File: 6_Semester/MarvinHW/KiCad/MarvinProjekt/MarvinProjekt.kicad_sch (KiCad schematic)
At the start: 27 parts, among them J1 Conn_02x03_Odd_Even, J2 Conn_01x04_Pin, SW1 SW_DPST_x2, SW2 SW_DPST_x2, SW3 SW_DPST_x2, SW4 SW_DPST_x2, SW5 SW_DPST_x2, SW6 SW_DPST_x2, U1 ESP32-S3-WROOM-1, U9 WS2812, X1 USB3.1C16PFSMT

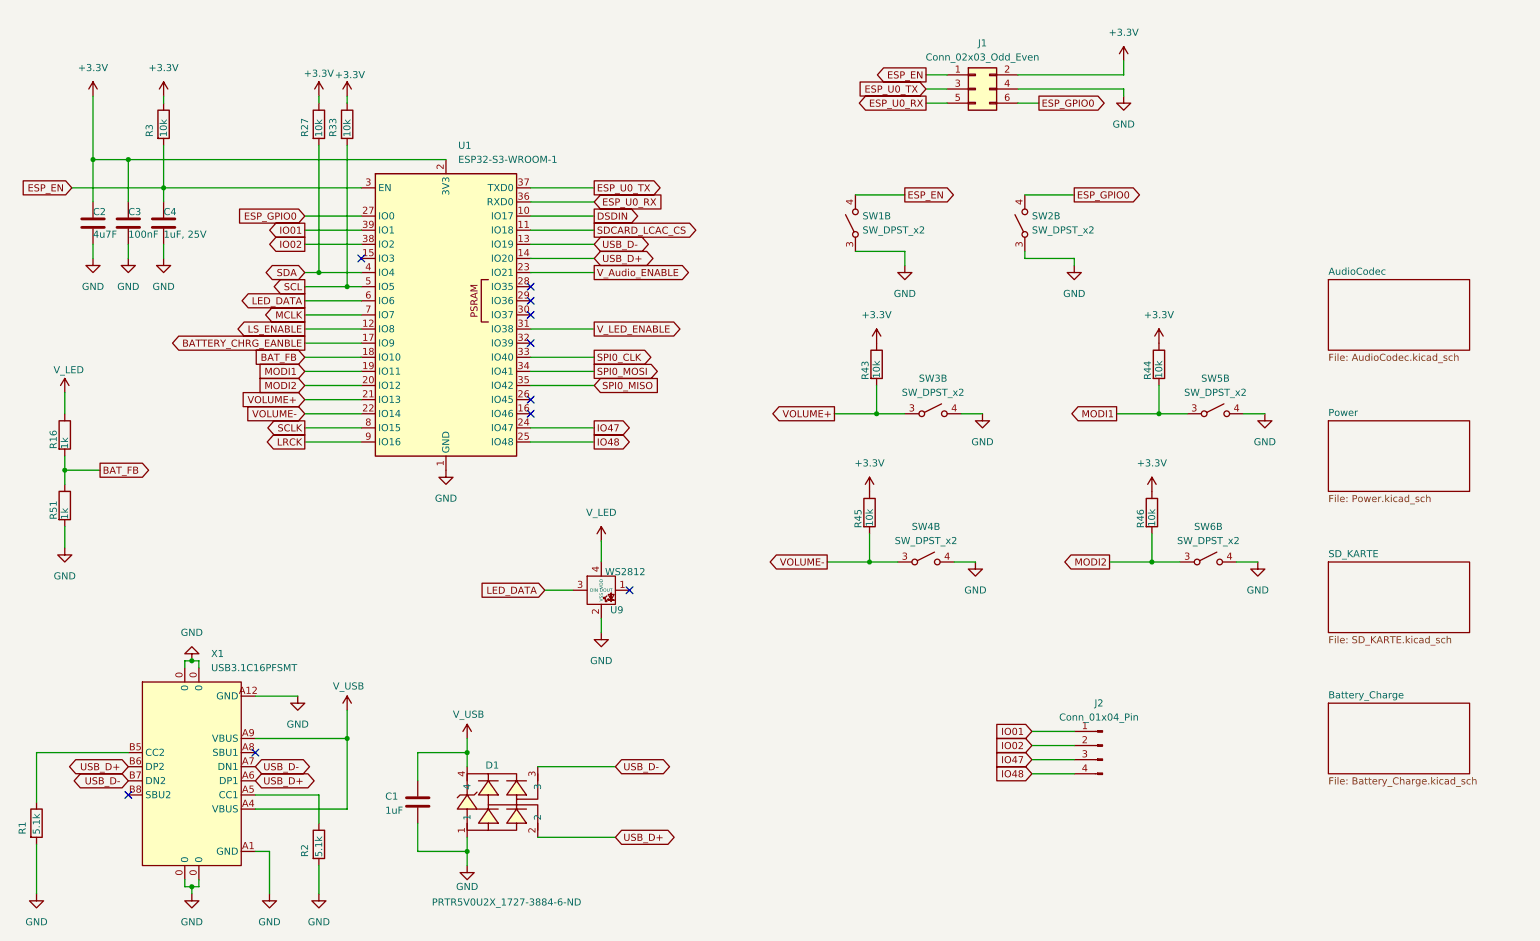
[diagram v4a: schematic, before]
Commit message: finished all footprints and put the objects in place
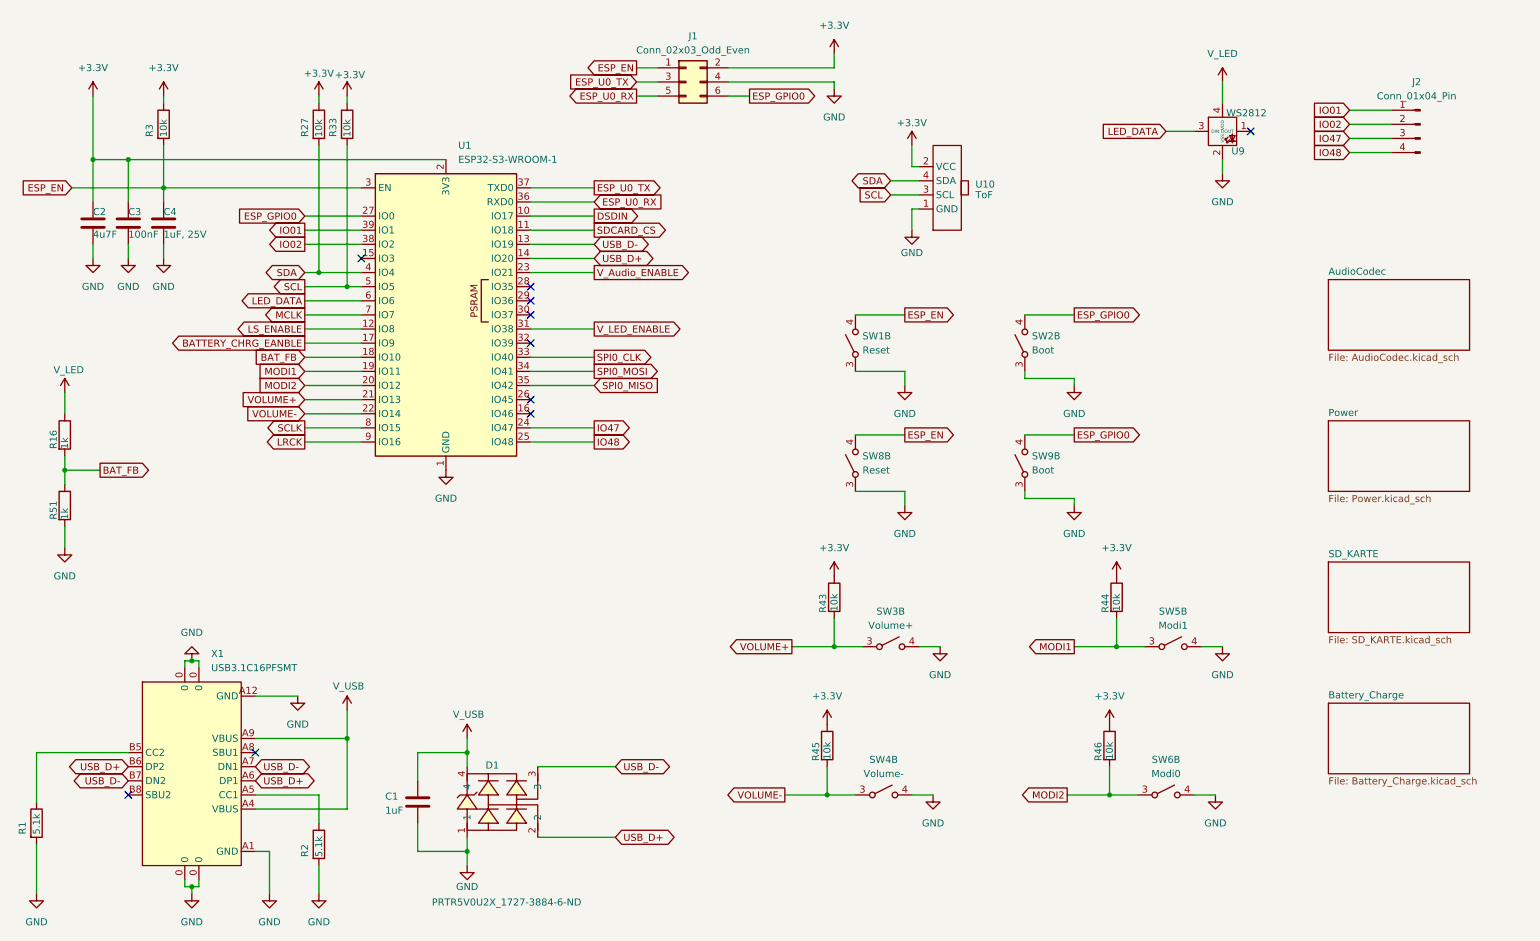
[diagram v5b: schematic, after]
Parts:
- added SW8: Reset, Library:Taster, symbol Switch:SW_DPST_x2
- added SW9: Boot, Library:Taster, symbol Switch:SW_DPST_x2
- added U10: ToF, Library:ToF, symbol Library:ToF
- SW1: value SW_DPST_x2 -> Reset; footprint Matrix2_Schnuppiprojekt:Taster -> Library:Taster
- SW2: value SW_DPST_x2 -> Boot; footprint Matrix2_Schnuppiprojekt:Taster -> Library:Taster
- SW3: value SW_DPST_x2 -> Volume+; footprint Matrix2_Schnuppiprojekt:Taster -> Library:Taster
- SW4: value SW_DPST_x2 -> Volume-; footprint Matrix2_Schnuppiprojekt:Taster -> Library:Taster
- SW5: value SW_DPST_x2 -> Modi1; footprint Matrix2_Schnuppiprojekt:Taster -> Library:Taster
- SW6: value SW_DPST_x2 -> Modi0; footprint Matrix2_Schnuppiprojekt:Taster -> Library:Taster
- X1: footprint Matrix2_Schnuppiprojekt:USB-C-SMD_TYPE-C-USB-17 -> Library:USB-C-SMD_TYPE-C-USB-17
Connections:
- net +3.3V: now also U10.2 (VCC)
- net ESP_EN: now also SW8.4 (B)
- net ESP_GPIO0: now also SW9.4 (B)
- net GND: now also SW8.3 (A), SW9.3 (A), U10.1 (GND)
- net SCL: now also U10.3 (SCL)
- net SDA: now also U10.4 (SDA)
- net SDCARD_LCAC_CS renamed SDCARD_CS
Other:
- moved on the sheet: J1, J2, R43, R44, R45, R46, SW1B, SW2B, SW3B, SW4B, SW5B, SW6B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

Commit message: Finished Layout
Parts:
- added C41, C42, C43, C44: 100nF, Capacitor_SMD:C_0805_2012Metric_Pad1.18x1.45mm_HandSolder, symbol Device:C
- added U11, U12, U13: WS2812, LED_SMD:LED_WS2812B-2020_PLCC4_2.0x2.0mm, symbol Library:WS2812
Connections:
- net BATTERY_CHRG_EANBLE is gone; now on net BAT_FB: U1.17 (IO9)
- net BAT_FB: no longer U1.18 (IO10)
- net GND: now also C41.2, C42.2, C43.2, C44.2, U11.2 (VSS), U12.2 (VSS), U13.2 (VSS)
- net MODI1: now also U1.22 (IO14); no longer U1.19 (IO11)
- net MODI2: now also U1.21 (IO13); no longer U1.20 (IO12)
- net VOLUME+: now also U1.20 (IO12); no longer U1.21 (IO13)
- net VOLUME-: now also U1.19 (IO11); no longer U1.22 (IO14)
- net V_LED: now also C41.1, C42.1, C43.1, C44.1, U11.4 (VDD), U12.4 (VDD), U13.4 (VDD)
- net at U9.1 (DOUT): now also U11.3 (DIN)
- new net: U12.1 (DOUT), U13.3 (DIN)
- new net: U11.1 (DOUT), U12.3 (DIN)
- new net ENABLE_BATTERY_CHRG: U1.18 (IO10)
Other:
- moved on the sheet: J2, U9

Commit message: deleted refrences and worked in errors from the drc
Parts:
- J1: now not fitted
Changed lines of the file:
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@@
 		(in_bom yes)
 		(on_board yes)
-		(dnp no)
+		(dnp yes)
 		(fields_autoplaced yes)
 		(property "Reference" "J1"

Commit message: add comonents to BoM
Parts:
- C1: LCSC Part C6119929 -> (none)
- C3, C41, C42, C43, C44: LCSC Part C38141 -> (none)
- C4: LCSC Part C344171 -> (none)
- R27, R3, R33: LCSC Part C5140188 -> (none)
